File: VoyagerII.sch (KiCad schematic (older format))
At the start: 14 parts, among them P1 TC2030-IDC, SW1 SW_PUSH, U1 ATXMEGA32A4U-AU, U2 MCP1700T-3002E/TT, U3 STF202-22T1G

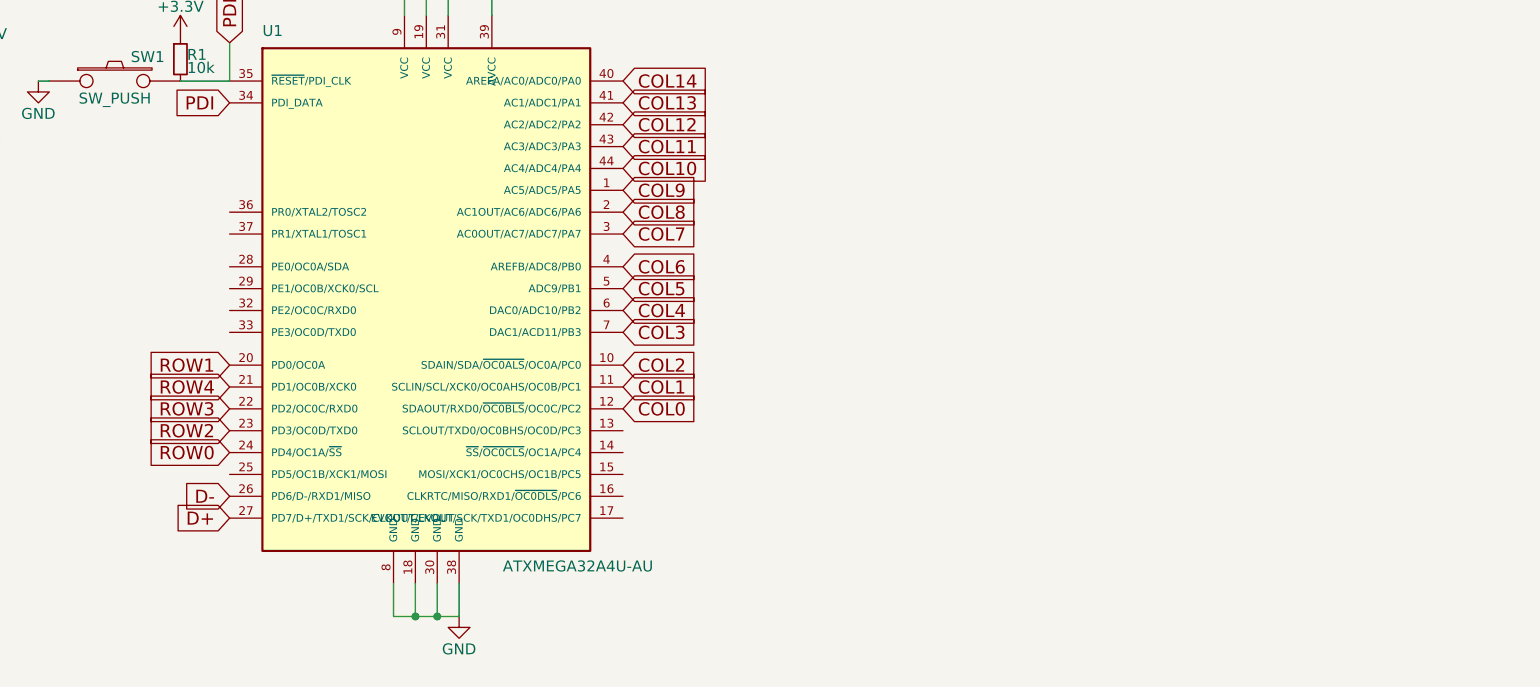
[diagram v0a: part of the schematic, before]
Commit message: Wire the LED controller
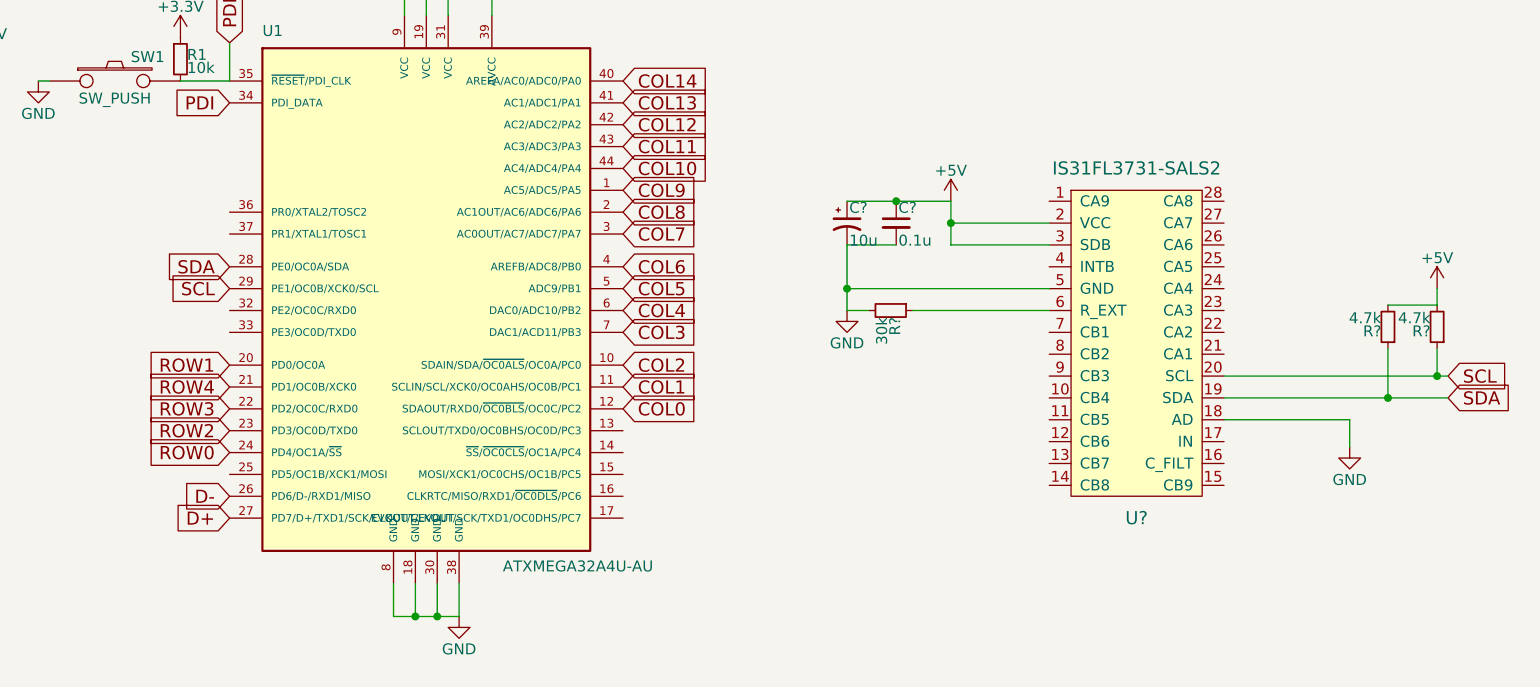
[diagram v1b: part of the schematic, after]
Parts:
- added C?: 0.1u, symbol C_Small
- added C?: 10u, symbol CP1_Small
- added R?: 30k, symbol R_Small
- added R? (x2): 4.7k, symbol R_Small
- added U?: IS31FL3731-SALS2, symbol IS31FL3731-SALS2
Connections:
- net +5V: now also C?.1, C?.1, R?.2, R?.2, U?.2 (VCC), U?.3 (SDB)
- net GND: now also C?.2, C?.2, R?.2, U?.18 (AD), U?.5 (GND)
- net SDA: now reaches U1.28 (PE0/OC0A/SDA)
- net SDA: now also R?.1, U?.19 (SDA)
- net SCL: now reaches U1.29 (PE1/OC0B/XCK0/SCL)
- net SCL: now also R?.1, U?.20 (SCL)
- new net: R?.1, U?.6 (R_EXT)
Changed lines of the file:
@@
 	1    0    0    -1
 $EndComp
-Wire Wire Line
-	4225 1300 4500 1300
-Connection ~ 4300 1300
-Wire Wire Line
-	2550 2500 2775 2500
-Wire Wire Line
-	2775 2500 2775 2325
-Wire Wire Line
-	3575 2200 3575 2050
-Wire Wire Line
-	3575 2050 3975 2050
-Wire Wire Line
-	3675 2050 3675 2200
-Wire Wire Line
-	3775 2050 3775 2200
-Connection ~ 3675 2050
-Wire Wire Line
-	3975 2050 3975 2200
-Connection ~ 3775 2050
-Wire Wire Line
-	3825 4950 3825 4800
-Wire Wire Line
-	3525 4950 3825 4950
-Wire Wire Line
-	3725 4950 3725 4800
-Wire Wire Line
-	3625 4950 3625 4800
-Connection ~ 3725 4950
-Wire Wire Line
-	3525 4950 3525 4800
-Connection ~ 3625 4950
-Wire Wire Line
-	725  3275 1550 3275
-Connection ~ 1325 3275
-Connection ~ 1125 3275
-Connection ~ 925  3275
-Wire Wire Line
-	725  3075 1550 3075
-Connection ~ 925  3075
-Connection ~ 1125 3075
-Connection ~ 1325 3075
-Wire Wire Line
-	3425 1300 3625 1300
-Wire Wire Line
-	1650 2625 1600 2625
 $Comp
 L +3.3V #PWR015
@@
 	1    0    0    -1
 $EndComp
-Wire Wire Line
-	1650 2425 1600 2425
 Text GLabel 2775 4200 0    60   Input ~ 0
 ROW0
@@
 	1    0    0    -1
 $EndComp
-Wire Wire Line
-	1425 1500 1825 1500
-Wire Wire Line
-	1825 1400 1425 1400
-Wire Wire Line
-	1825 1300 1825 1200
 $Comp
 L GND #PWR016
@@
 	1    0    0    -1
 $EndComp
-Wire Wire Line
-	2625 1300 2675 1300
-Wire Wire Line
-	2675 1300 2675 1200
-Wire Wire Line
-	2675 1200 2775 1200
-Wire Wire Line
-	2900 1400 2625 1400
-Wire Wire Line
-	2900 1500 2625 1500
-Wire Wire Line
-	1475 1250 1475 1300
-Wire Wire Line
-	1425 1300 1550 1300
-Connection ~ 1475 1300
-Wire Wire Line
-	1750 1300 1825 1300
-Wire Wire Line
-	1900 2500 1950 2500
 $Sheet
 S 1350 6100 1900 875
@@
 F1 "Matrix.sch" 60
 $EndSheet
+$Comp
+L IS31FL3731-SALS2 U?
+U 1 1 5A64C5D4
+P 6925 3700
+F 0 "U?" H 6925 2900 60  0000 C CNN
+F 1 "IS31FL3731-SALS2" H 6925 4500 60  0000 C CNN
+F 2 "" H 6925 3700 60  0001 C CNN
+F 3 "" H 6925 3700 60  0001 C CNN
+	1    6925 3700
+	1    0    0    -1
+$EndComp
+$Comp
+L R_Small R?
+U 1 1 5A64D7FB
+P 5800 3550
+F 0 "R?" H 5830 3570 50  0000 L CNN
+F 1 "30k" H 5830 3510 50  0000 L CNN
+F 2 "" H 5800 3550 50  0001 C CNN
+F 3 "" H 5800 3550 50  0001 C CNN
+	1    5800 3550
+	0    1    1    0
+$EndComp
+$Comp
+L GND #PWR?
+U 1 1 5A64D83E
+P 5600 3550
+F 0 "#PWR?" H 5600 3300 50  0001 C CNN
+F 1 "GND" H 5600 3400 50  0000 C CNN
+F 2 "" H 5600 3550 50  0001 C CNN
+F 3 "" H 5600 3550 50  0001 C CNN
+	1    5600 3550
+	1    0    0    -1
+$EndComp
+Text GLabel 8350 3950 2    60   Input ~ 0
+SDA
+Text GLabel 8350 3850 2    60   Input ~ 0
+SCL
+Text GLabel 2775 3350 0    60   Input ~ 0
+SDA
+Text GLabel 2775 3450 0    60   Input ~ 0
+SCL
+$Comp
+L +5V #PWR?
+U 1 1 5A64EBF7
+P 6075 3050
+F 0 "#PWR?" H 6075 2900 50  0001 C CNN
+F 1 "+5V" H 6075 3190 50  0000 C CNN
+F 2 "" H 6075 3050 50  0001 C CNN
+F 3 "" H 6075 3050 50  0001 C CNN
+	1    6075 3050
+	1    0    0    -1
+$EndComp
+$Comp
+L C_Small C?
+U 1 1 5A64EFE3
+P 5825 3150
+F 0 "C?" H 5835 3220 50  0000 L CNN
+F 1 "0.1u" H 5835 3070 50  0000 L CNN
+F 2 "" H 5825 3150 50  0001 C CNN
+F 3 "" H 5825 3150 50  0001 C CNN
+	1    5825 3150
+	1    0    0    -1
+$EndComp
+$Comp
+L CP1_Small C?
+U 1 1 5A64F032
+P 5600 3150
+F 0 "C?" H 5610 3220 50  0000 L CNN
+F 1 "10u" H 5610 3070 50  0000 L CNN
+F 2 "" H 5600 3150 50  0001 C CNN
+F 3 "" H 5600 3150 50  0001 C CNN
+	1    5600 3150
+	1    0    0    -1
+$EndComp
+Wire Wire Line
+	4225 1300 4500 1300
+Connection ~ 4300 1300
+Wire Wire Line
+	2550 2500 2775 2500
+Wire Wire Line
+	2775 2500 2775 2325
+Wire Wire Line
+	3575 2200 3575 2050
+Wire Wire Line
+	3575 2050 3975 2050
+Wire Wire Line
+	3675 2050 3675 2200
+Wire Wire Line
+	3775 2050 3775 2200
+Connection ~ 3675 2050
+Wire Wire Line
+	3975 2050 3975 2200
+Connection ~ 3775 2050
+Wire Wire Line
+	3825 4950 3825 4800
+Wire Wire Line
+	3525 4950 3825 4950
+Wire Wire Line
+	3725 4950 3725 4800
+Wire Wire Line
+	3625 4950 3625 4800
+Connection ~ 3725 4950
+Wire Wire Line
+	3525 4950 3525 4800
+Connection ~ 3625 4950
+Wire Wire Line
+	725  3275 1550 3275
+Connection ~ 1325 3275
+Connection ~ 1125 3275
+Connection ~ 925  3275
+Wire Wire Line
+	725  3075 1550 3075
+Connection ~ 925  3075
+Connection ~ 1125 3075
+Connection ~ 1325 3075
+Wire Wire Line
+	3425 1300 3625 1300
+Wire Wire Line
+	1650 2625 1600 2625
+Wire Wire Line
+	1650 2425 1600 2425
+Wire Wire Line
+	1425 1500 1825 1500
+Wire Wire Line
+	1825 1400 1425 1400
+Wire Wire Line
+	1825 1300 1825 1200
+Wire Wire Line
+	2625 1300 2675 1300
+Wire Wire Line
+	2675 1300 2675 1200
+Wire Wire Line
+	2675 1200 2775 1200
+Wire Wire Line
+	2900 1400 2625 1400
+Wire Wire Line
+	2900 1500 2625 1500
+Wire Wire Line
+	1475 1250 1475 1300
+Wire Wire Line
+	1425 1300 1550 1300
+Connection ~ 1475 1300
+Wire Wire Line
+	1750 1300 1825 1300
+Wire Wire Line
+	1900 2500 1950 2500
+Wire Wire Line
+	6525 3150 6075 3150
+Wire Wire Line
+	6075 3050 6075 3250
+Wire Wire Line
+	6075 3250 6525 3250
+Connection ~ 6075 3150
+Wire Wire Line
+	6525 3550 5900 3550
+Wire Wire Line
+	5600 3550 5700 3550
+Wire Wire Line
+	7325 3950 8350 3950
+Wire Wire Line
+	7325 3850 8350 3850
+Wire Wire Line
+	5600 3250 5825 3250
+Wire Wire Line
+	5600 3250 5600 3550
+Wire Wire Line
+	5600 3050 6075 3050
+Connection ~ 5825 3050
+Wire Wire Line
+	6525 3450 5600 3450
+Connection ~ 5600 3450
+Wire Wire Line
+	7325 4050 7900 4050
+Wire Wire Line
+	7900 4050 7900 4175
+$Comp
+L GND #PWR?
+U 1 1 5A64FC3C
+P 7900 4175
+F 0 "#PWR?" H 7900 3925 50  0001 C CNN
+F 1 "GND" H 7900 4025 50  0000 C CNN
+F 2 "" H 7900 4175 50  0001 C CNN
+F 3 "" H 7900 4175 50  0001 C CNN
+	1    7900 4175
+	1    0    0    -1
+$EndComp
+$Comp
+L R_Small R?
+U 1 1 5A650846
+P 8075 3625
+F 0 "R?" H 8105 3645 50  0000 L CNN
+F 1 "4.7k" H 8105 3585 50  0000 L CNN
+F 2 "" H 8075 3625 50  0001 C CNN
+F 3 "" H 8075 3625 50  0001 C CNN
+	1    8075 3625
+	-1   0    0    1
+$EndComp
+$Comp
+L R_Small R?
+U 1 1 5A650C5F
+P 8300 3625
+F 0 "R?" H 8330 3645 50  0000 L CNN
+F 1 "4.7k" H 8330 3585 50  0000 L CNN
+F 2 "" H 8300 3625 50  0001 C CNN
+F 3 "" H 8300 3625 50  0001 C CNN
+	1    8300 3625
+	-1   0    0    1
+$EndComp
+Wire Wire Line
+	8300 3725 8300 3850
+Connection ~ 8300 3850
+Wire Wire Line
+	8075 3725 8075 3950
+Connection ~ 8075 3950
+Wire Wire Line
+	8075 3525 8300 3525
+Wire Wire Line
+	8300 3525 8300 3450
+$Comp
+L +5V #PWR?
+U 1 1 5A650E24
+P 8300 3450
+F 0 "#PWR?" H 8300 3300 50  0001 C CNN
+F 1 "+5V" H 8300 3590 50  0000 C CNN
+F 2 "" H 8300 3450 50  0001 C CNN
+F 3 "" H 8300 3450 50  0001 C CNN
+	1    8300 3450
+	1    0    0    -1
+$EndComp
 $EndSCHEMATC

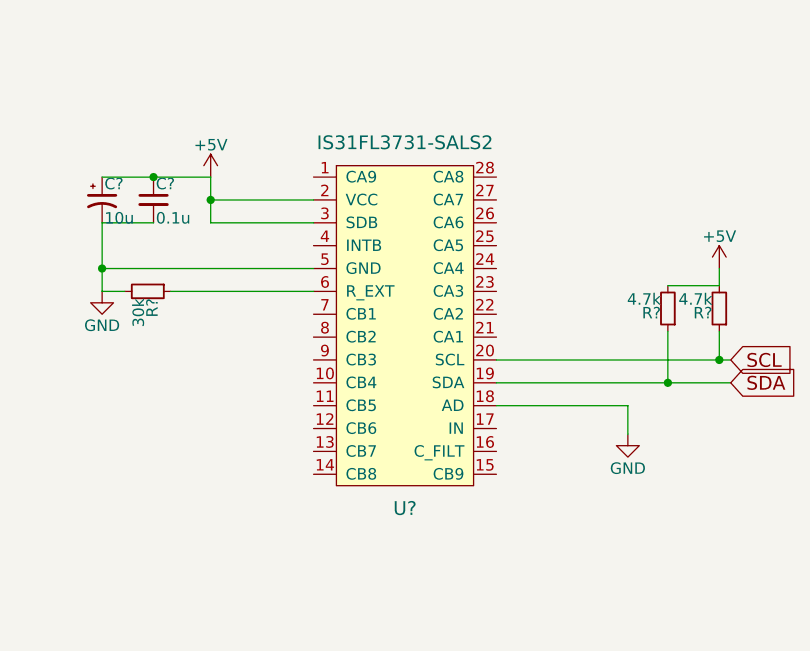
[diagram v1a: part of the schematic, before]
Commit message: Add LED matrix labels
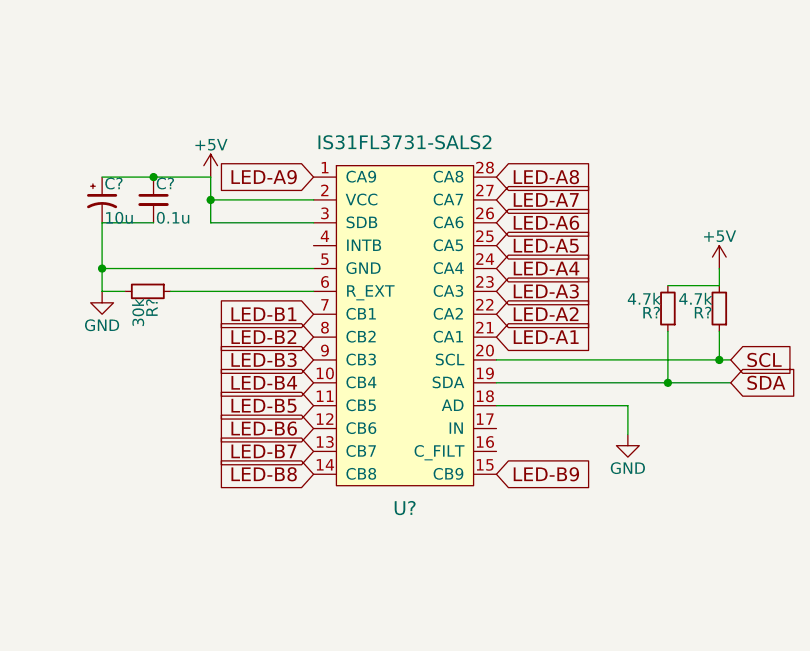
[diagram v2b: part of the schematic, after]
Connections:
- net LED-A9: now reaches U?.1 (CA9)
- net LED-B4: now reaches U?.10 (CB4)
- net LED-B5: now reaches U?.11 (CB5)
- net LED-B6: now reaches U?.12 (CB6)
- net LED-B7: now reaches U?.13 (CB7)
- net LED-B8: now reaches U?.14 (CB8)
- net LED-B9: now reaches U?.15 (CB9)
- net LED-A1: now reaches U?.21 (CA1)
- net LED-A2: now reaches U?.22 (CA2)
- net LED-A3: now reaches U?.23 (CA3)
- net LED-A4: now reaches U?.24 (CA4)
- net LED-A5: now reaches U?.25 (CA5)
- net LED-A6: now reaches U?.26 (CA6)
- net LED-A7: now reaches U?.27 (CA7)
- net LED-A8: now reaches U?.28 (CA8)
- net LED-B1: now reaches U?.7 (CB1)
- net LED-B2: now reaches U?.8 (CB2)
- net LED-B3: now reaches U?.9 (CB3)
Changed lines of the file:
@@
 	1    0    0    -1
 $EndComp
+Text GLabel 7325 3750 2    60   Input ~ 0
+LED-A1
+Text GLabel 7325 3650 2    60   Input ~ 0
+LED-A2
+Text GLabel 7325 3550 2    60   Input ~ 0
+LED-A3
+Text GLabel 7325 3450 2    60   Input ~ 0
+LED-A4
+Text GLabel 7325 3350 2    60   Input ~ 0
+LED-A5
+Text GLabel 7325 3250 2    60   Input ~ 0
+LED-A6
+Text GLabel 7325 3150 2    60   Input ~ 0
+LED-A7
+Text GLabel 7325 3050 2    60   Input ~ 0
+LED-A8
+Text GLabel 6525 3050 0    60   Input ~ 0
+LED-A9
+Text GLabel 6525 3650 0    60   Input ~ 0
+LED-B1
+Text GLabel 6525 3750 0    60   Input ~ 0
+LED-B2
+Text GLabel 6525 3850 0    60   Input ~ 0
+LED-B3
+Text GLabel 6525 3950 0    60   Input ~ 0
+LED-B4
+Text GLabel 6525 4050 0    60   Input ~ 0
+LED-B5
+Text GLabel 6525 4150 0    60   Input ~ 0
+LED-B6
+Text GLabel 6525 4250 0    60   Input ~ 0
+LED-B7
+Text GLabel 6525 4350 0    60   Input ~ 0
+LED-B8
+Text GLabel 7325 4350 2    60   Input ~ 0
+LED-B9
 $EndSCHEMATC

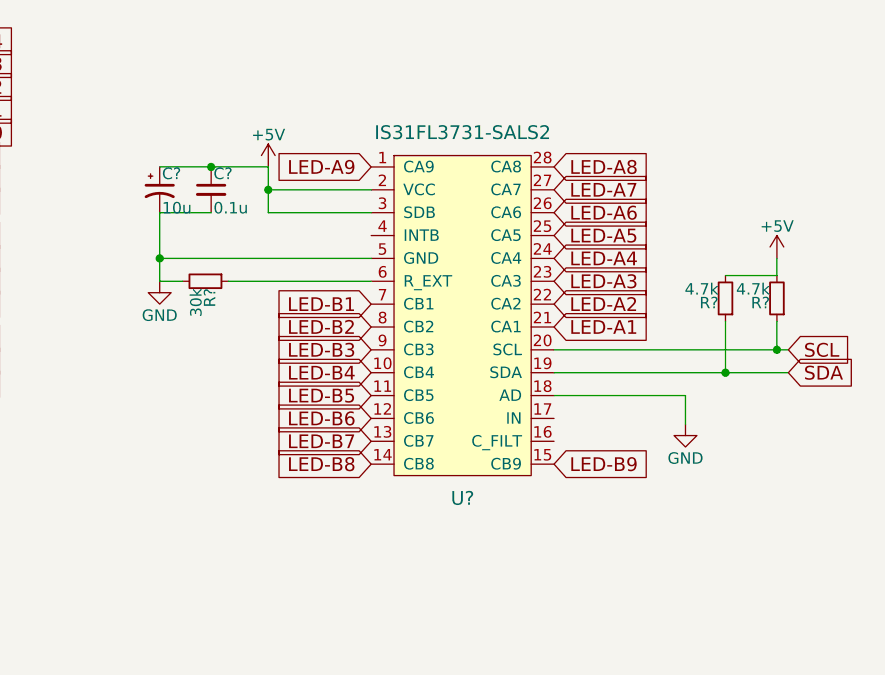
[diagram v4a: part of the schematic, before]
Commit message: Assign footprints, along with placeholders for mx
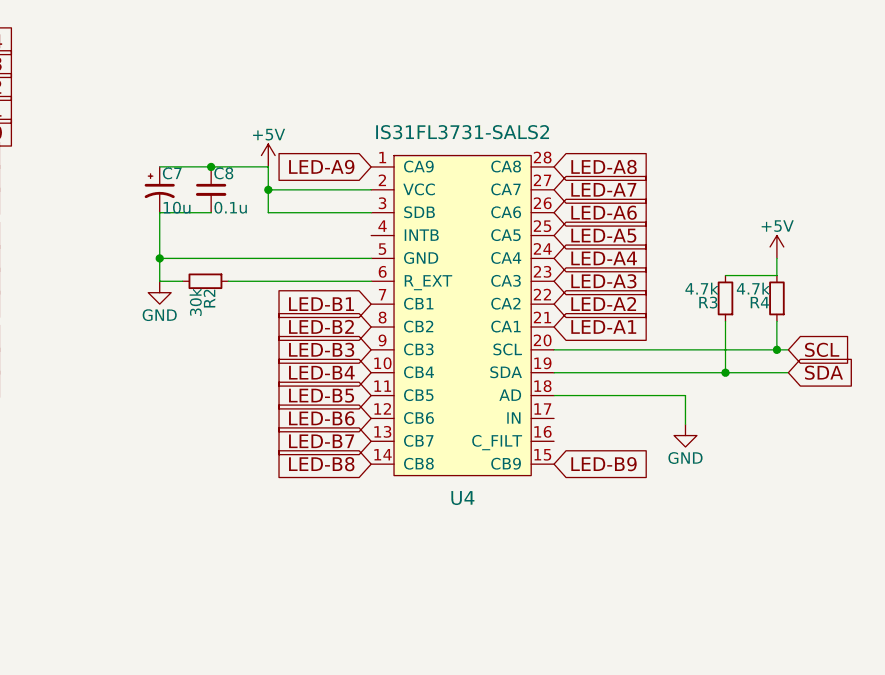
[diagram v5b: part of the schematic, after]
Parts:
- C7, C8: renamed from C?; footprint (none) -> Capacitors_SMD:C_0805
- P1: footprint (none) -> Tag-Connect:TC2030-NL_SMALL_AND_IDC_PDI
- R2, R3, R4: renamed from R?; footprint (none) -> Resistors_SMD:R_0805
- U4: renamed from U?; footprint (none) -> Housings_SSOP:SSOP-28_5.3x10.2mm_Pitch0.65mm
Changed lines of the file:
@@
 F 0 "P1" H 1300 2325 40  0000 L CNN
 F 1 "TC2030-IDC" H 1350 2725 40  0000 C CNN
-F 2 "" H 1350 2525 60  0001 C CNN
+F 2 "Tag-Connect:TC2030-NL_SMALL_AND_IDC_PDI" H 1350 2525 60  0001 C CNN
 F 3 "" H 1350 2525 60  0000 C CNN
 	1    1350 2525
@@
 $EndSheet
 $Comp
-L IS31FL3731-SALS2 U?
+L IS31FL3731-SALS2 U4
 U 1 1 5A64C5D4
 P 6925 3700
-F 0 "U?" H 6925 2900 60  0000 C CNN
+F 0 "U4" H 6925 2900 60  0000 C CNN
 F 1 "IS31FL3731-SALS2" H 6925 4500 60  0000 C CNN
-F 2 "" H 6925 3700 60  0001 C CNN
+F 2 "Housings_SSOP:SSOP-28_5.3x10.2mm_Pitch0.65mm" H 6925 3700 60  0001 C CNN
 F 3 "" H 6925 3700 60  0001 C CNN
 	1    6925 3700
@@
 $EndComp
 $Comp
-L R_Small R?
+L R_Small R2
 U 1 1 5A64D7FB
 P 5800 3550
-F 0 "R?" H 5830 3570 50  0000 L CNN
+F 0 "R2" H 5830 3570 50  0000 L CNN
 F 1 "30k" H 5830 3510 50  0000 L CNN
-F 2 "" H 5800 3550 50  0001 C CNN
+F 2 "Resistors_SMD:R_0805" H 5800 3550 50  0001 C CNN
 F 3 "" H 5800 3550 50  0001 C CNN
 	1    5800 3550
@@
 $EndComp
 $Comp
-L GND #PWR?
+L GND #PWR017
 U 1 1 5A64D83E
 P 5600 3550
-F 0 "#PWR?" H 5600 3300 50  0001 C CNN
+F 0 "#PWR017" H 5600 3300 50  0001 C CNN
 F 1 "GND" H 5600 3400 50  0000 C CNN
 F 2 "" H 5600 3550 50  0001 C CNN
@@
 SCL
 $Comp
-L +5V #PWR?
+L +5V #PWR018
 U 1 1 5A64EBF7
 P 6075 3050
-F 0 "#PWR?" H 6075 2900 50  0001 C CNN
+F 0 "#PWR018" H 6075 2900 50  0001 C CNN
 F 1 "+5V" H 6075 3190 50  0000 C CNN
 F 2 "" H 6075 3050 50  0001 C CNN
@@
 $EndComp
 $Comp
-L C_Small C?
+L C_Small C8
 U 1 1 5A64EFE3
 P 5825 3150
-F 0 "C?" H 5835 3220 50  0000 L CNN
+F 0 "C8" H 5835 3220 50  0000 L CNN
 F 1 "0.1u" H 5835 3070 50  0000 L CNN
-F 2 "" H 5825 3150 50  0001 C CNN
+F 2 "Capacitors_SMD:C_0805" H 5825 3150 50  0001 C CNN
 F 3 "" H 5825 3150 50  0001 C CNN
 	1    5825 3150
@@
 $EndComp
 $Comp
-L CP1_Small C?
+L CP1_Small C7
 U 1 1 5A64F032
 P 5600 3150
-F 0 "C?" H 5610 3220 50  0000 L CNN
+F 0 "C7" H 5610 3220 50  0000 L CNN
 F 1 "10u" H 5610 3070 50  0000 L CNN
-F 2 "" H 5600 3150 50  0001 C CNN
+F 2 "Capacitors_SMD:C_0805" H 5600 3150 50  0001 C CNN
 F 3 "" H 5600 3150 50  0001 C CNN
 	1    5600 3150
@@
 	7900 4050 7900 4175
 $Comp
-L GND #PWR?
+L GND #PWR019
 U 1 1 5A64FC3C
 P 7900 4175
-F 0 "#PWR?" H 7900 3925 50  0001 C CNN
+F 0 "#PWR019" H 7900 3925 50  0001 C CNN
 F 1 "GND" H 7900 4025 50  0000 C CNN
 F 2 "" H 7900 4175 50  0001 C CNN
@@
 $EndComp
 $Comp
-L R_Small R?
+L R_Small R3
 U 1 1 5A650846
 P 8075 3625
-F 0 "R?" H 8105 3645 50  0000 L CNN
+F 0 "R3" H 8105 3645 50  0000 L CNN
 F 1 "4.7k" H 8105 3585 50  0000 L CNN
-F 2 "" H 8075 3625 50  0001 C CNN
+F 2 "Resistors_SMD:R_0805" H 8075 3625 50  0001 C CNN
 F 3 "" H 8075 3625 50  0001 C CNN
 	1    8075 3625
@@
 $EndComp
 $Comp
-L R_Small R?
+L R_Small R4
 U 1 1 5A650C5F
 P 8300 3625
-F 0 "R?" H 8330 3645 50  0000 L CNN
+F 0 "R4" H 8330 3645 50  0000 L CNN
 F 1 "4.7k" H 8330 3585 50  0000 L CNN
-F 2 "" H 8300 3625 50  0001 C CNN
+F 2 "Resistors_SMD:R_0805" H 8300 3625 50  0001 C CNN
 F 3 "" H 8300 3625 50  0001 C CNN
 	1    8300 3625
@@
 	8300 3525 8300 3450
 $Comp
-L +5V #PWR?
+L +5V #PWR020
 U 1 1 5A650E24
 P 8300 3450
-F 0 "#PWR?" H 8300 3300 50  0001 C CNN
+F 0 "#PWR020" H 8300 3300 50  0001 C CNN
 F 1 "+5V" H 8300 3590 50  0000 C CNN
 F 2 "" H 8300 3450 50  0001 C CNN
